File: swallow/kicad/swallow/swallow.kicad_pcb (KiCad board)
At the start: 2 copper layers, 75.8 x 74.2 mm, 36 parts, among them J1 Raspberry Pi 3/4 B, J10 evens, J2 echo2, J3 ground, J4 VCC, J5 echo3, J6 echo4, J7 echo1, J8 power terminal, J9 odds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

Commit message: ++ - kamangir/bolt#746
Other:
- outline, holes or cut-outs redrawn
- board text added: "swallow - v14 Karband / Kamangir"
- board text removed: "swallow - v10 Karband / Kamangir"
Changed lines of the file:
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@@
 	)
 	(gr_circle
-		(center 190.9 117.3)
-		(end 191.8 118.2)
+		(center 190.9 120.8)
+		(end 191.8 121.7)
 		(stroke
 			(width 0.05)
@@
 	)
 	(gr_circle
-		(center 132.9 117.3)
-		(end 133.8 118.2)
+		(center 132.9 120.8)
+		(end 133.8 121.7)
 		(stroke
 			(width 0.05)
@@
 	)
 	(gr_circle
-		(center 132.9 117.3)
-		(end 134.4 114.6)
+		(center 132.9 120.8)
+		(end 134.4 118.1)
 		(stroke
 			(width 0.1)
@@
 	)
 	(gr_circle
-		(center 190.9 117.3)
-		(end 193.1 119.4)
+		(center 190.9 120.8)
+		(end 193.1 122.9)
 		(stroke
 			(width 0.1)
@@
 		)
 	)
-	(gr_text "swallow - v10\nKarband / Kamangir"
+	(gr_text "swallow - v14\nKarband / Kamangir"
 		(at 158.6 63.1 0)
 		(layer "F.SilkS")
@@
 		(layer "User.1")
 		(pts
-			(xy 132.9 117.3) (xy 112.7 87.9)
-		)
-		(height -29.8)
-		(orientation 1)
-		(format
-			(prefix "")
-			(suffix "")
-			(units 3)
-			(units_format 0)
-			(precision 4)
-			(suppress_zeroes yes)
-		)
-		(style
-			(thickness 0.2)
-			(arrow_length 1.27)
-			(text_position_mode 0)
-			(arrow_direction outward)
-			(extension_height 0.58642)
-			(extension_offset 0.5)
-			(keep_text_aligned yes)
-		)
-		(gr_text "29.4"
-			(at 101.95 102.6 90)
-			(layer "User.1")
-			(effects
-				(font
-					(size 1 1)
-					(thickness 0.15)
-				)
-			)
-		)
-	)
-	(dimension
-		(type orthogonal)
-		(layer "User.1")
-		(pts
-			(xy 132.9 71.8) (xy 132.9 117.3)
+			(xy 132.9 71.8) (xy 132.9 120.8)
 		)
 		(height -26.1)
@@
 			(keep_text_aligned yes)
 		)
-		(gr_text "45.5"
-			(at 105.65 94.55 90)
+		(gr_text "49"
+			(at 105.65 96.3 90)
 			(layer "User.1")
 			(effects
@@
 		(layer "User.1")
 		(pts
+			(xy 112.7 87.9) (xy 106.8 120.8)
+		)
+		(height -9.6)
+		(orientation 1)
+		(format
+			(prefix "")
+			(suffix "")
+			(units 3)
+			(units_format 0)
+			(precision 4)
+			(suppress_zeroes yes)
+		)
+		(style
+			(thickness 0.2)
+			(arrow_length 1.27)
+			(text_position_mode 0)
+			(arrow_direction outward)
+			(extension_height 0.58642)
+			(extension_offset 0.5)
+			(keep_text_aligned yes)
+		)
+		(gr_text "32.9"
+			(at 101.95 104.35 90)
+			(layer "User.1")
+			(effects
+				(font
+					(size 1 1)
+					(thickness 0.15)
+				)
+			)
+		)
+	)
+	(dimension
+		(type orthogonal)
+		(layer "User.1")
+		(pts
 			(xy 187.838954 71.8) (xy 193.961046 71.8)
 		)
@@
 		(layer "User.1")
 		(pts
-			(xy 190.9 117.3) (xy 190.9 71.8)
+			(xy 190.9 120.8) (xy 190.9 71.8)
 		)
 		(height 13.6)
@@
 			(keep_text_aligned yes)
 		)
-		(gr_text "45.5"
-			(at 203.35 94.55 90)
-			(layer "User.1")
-			(effects
+		(gr_text "49"
+			(at 203.35 96.3 90)
+			(layer "User.1")
+			(effects

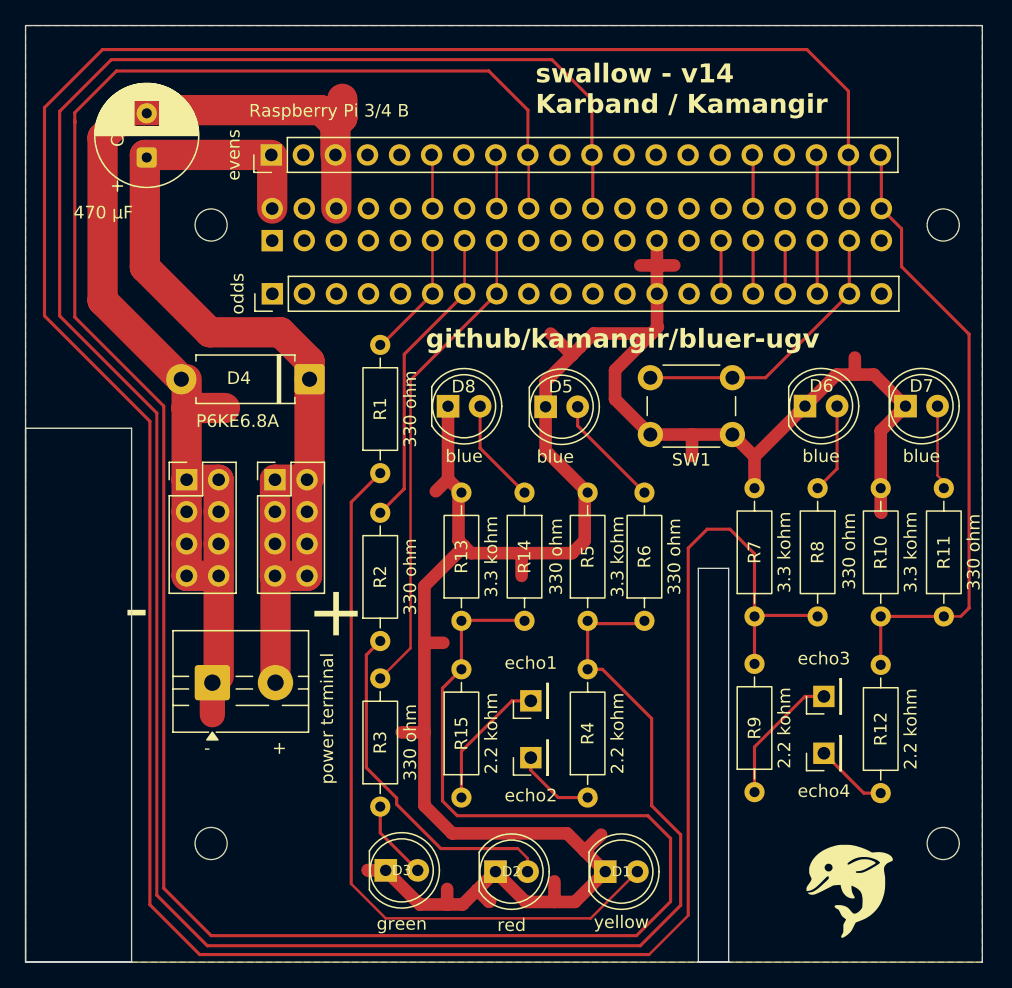
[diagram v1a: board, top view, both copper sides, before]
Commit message: fix - kamangir/bolt#746
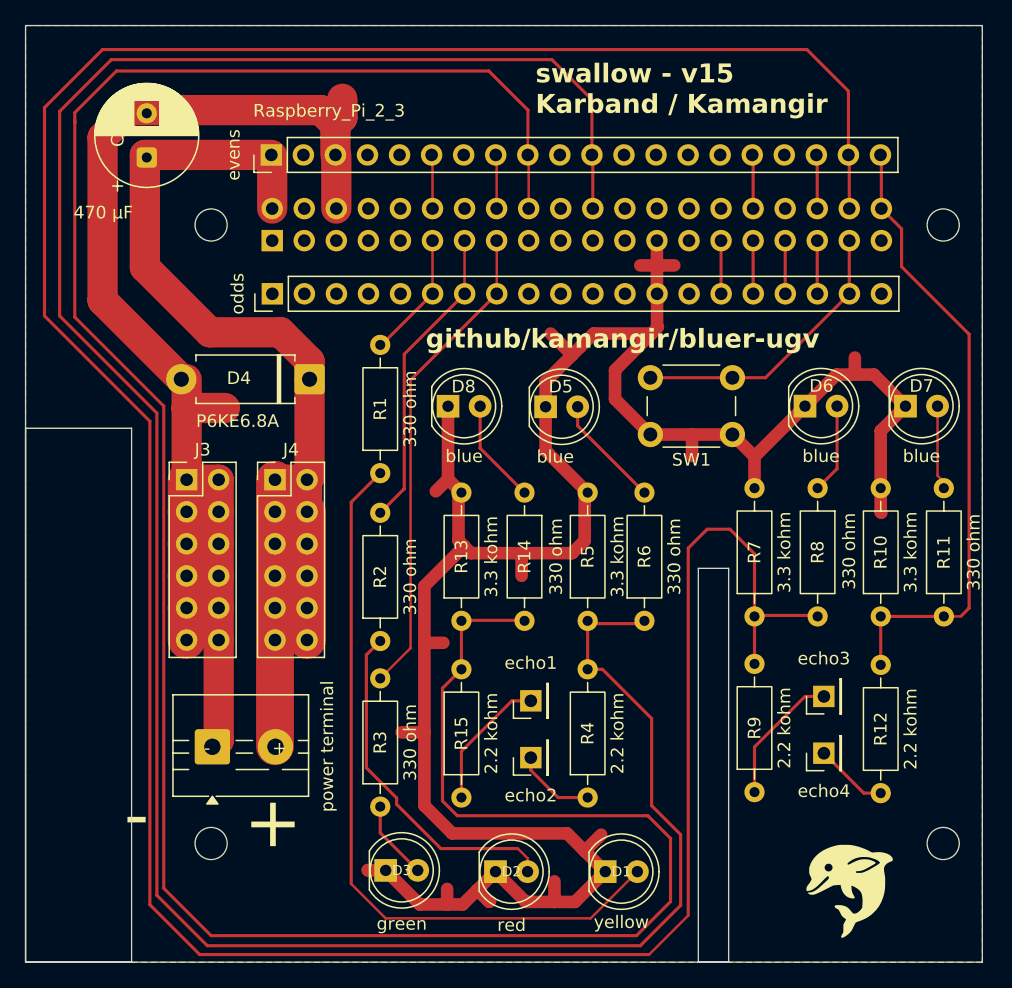
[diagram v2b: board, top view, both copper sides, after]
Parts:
- J1: value Raspberry Pi 3/4 B -> Raspberry_Pi_2_3
- J3, J4: footprint Connector_PinHeader_2.54mm:PinHeader_2x04_P2.54mm_Vertical -> Connector_PinHeader_2.54mm:PinHeader_2x06_P2.54mm_Vertical
- moved J8 5.08 mm to (133.0, 113.1)
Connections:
- C1 pad 2: GND -> Net-(D1-K)
- D1 pad 1: GND -> Net-(D1-K)
- D2 pad 1: GND -> Net-(D1-K)
- D3 pad 1: GND -> Net-(D1-K)
- D4 pad 2: GND -> Net-(D1-K)
- D5 pad 1: GND -> Net-(D1-K)
- D6 pad 1: GND -> Net-(D1-K)
- D7 pad 1: GND -> Net-(D1-K)
- D8 pad 1: GND -> Net-(D1-K)
- J1 pad 25: GND -> Net-(D1-K)
- J1 pad 6: GND -> Net-(D1-K)
- J10 pad 3: GND -> Net-(D1-K)
- J3 pad 1: GND -> Net-(D1-K)
- J3 pad 2: GND -> Net-(D1-K)
- J3 pad 3: GND -> Net-(D1-K)
- J3 pad 4: GND -> Net-(D1-K)
- J3 pad 5: GND -> Net-(D1-K)
- J3 pad 6: GND -> Net-(D1-K)
- J3 pad 7: GND -> Net-(D1-K)
- J3 pad 8: GND -> Net-(D1-K)
- J8 pad 1: GND -> Net-(D1-K)
- J9 pad 13: GND -> Net-(D1-K)
- R10 pad 2: GND -> Net-(D1-K)
- R13 pad 2: GND -> Net-(D1-K)
- R5 pad 2: GND -> Net-(D1-K)
- R7 pad 2: GND -> Net-(D1-K)
- SW1 pad 1: GND -> Net-(D1-K)
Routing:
- net Net-(D1-K): track 0.00 -> 284.5 mm
- net GND: track 276.1 -> 0.00 mm
- net Net-(D4-K): track 77.7 -> 87.9 mm
- added copper zone on F.Cu, net Net-(D1-K)
- removed copper zone on F.Cu, net GND
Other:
- board text added: "swallow - v15 Karband / Kamangir"
- board text removed: "swallow - v14 Karband / Kamangir"

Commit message: ++ - kamangir/bolt#746
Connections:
- C1 pad 1: Net-(D4-K) -> /pin2
- C1 pad 2: Net-(D1-K) -> /pin14
- D1 pad 1: Net-(D1-K) -> /pin14
- D2 pad 1: Net-(D1-K) -> /pin14
- D3 pad 1: Net-(D1-K) -> /pin14
- D4 pad 1: Net-(D4-K) -> /pin2
- D4 pad 2: Net-(D1-K) -> /pin14
- D5 pad 1: Net-(D1-K) -> /pin14
- D6 pad 1: Net-(D1-K) -> /pin14
- D7 pad 1: Net-(D1-K) -> /pin14
- D8 pad 1: Net-(D1-K) -> /pin14
- J1 pad 1: Net-(J1-3V3-Pad1) -> /pin1
- J1 pad 10: unconnected-(J1-GPIO15/RXD-Pad10) -> /pin10
- J1 pad 14: Net-(D1-K) -> /pin14
- J1 pad 17: Net-(J1-3V3-Pad1) -> /pin1
- J1 pad 19: unconnected-(J1-MOSI0/GPIO10-Pad19) -> /pin19
- J1 pad 2: Net-(D4-K) -> /pin2
- J1 pad 20: Net-(D1-K) -> /pin14
- J1 pad 21: unconnected-(J1-MISO0/GPIO9-Pad21) -> /pin21
- J1 pad 23: unconnected-(J1-SCLK0/GPIO11-Pad23) -> /pin23
- J1 pad 24: unconnected-(J1-~{CE0}/GPIO8-Pad24) -> /pin24
- J1 pad 25: Net-(D1-K) -> /pin14
- J1 pad 26: unconnected-(J1-~{CE1}/GPIO7-Pad26) -> /pin26
- J1 pad 27: unconnected-(J1-ID_SD/GPIO0-Pad27) -> /pin27
- J1 pad 28: unconnected-(J1-ID_SC/GPIO1-Pad28) -> /pin28
- J1 pad 3: unconnected-(J1-SDA/GPIO2-Pad3) -> /pin3
- J1 pad 30: Net-(D1-K) -> /pin14
- J1 pad 34: Net-(D1-K) -> /pin14
- J1 pad 39: Net-(D1-K) -> /pin14
- J1 pad 4: Net-(D4-K) -> /pin2
- J1 pad 5: unconnected-(J1-SCL/GPIO3-Pad5) -> /pin5
- J1 pad 6: Net-(D1-K) -> /pin14
- J1 pad 7: unconnected-(J1-GCLK0/GPIO4-Pad7) -> /pin7
- J1 pad 8: unconnected-(J1-GPIO14/TXD-Pad8) -> /pin8
- J1 pad 9: Net-(D1-K) -> /pin14
- J10 pad 1: Net-(D4-K) -> /pin2
- J10 pad 10: unconnected-(J10-Pin_10-Pad10) -> /pin14
- J10 pad 12: unconnected-(J10-Pin_12-Pad12) -> /pin24
- J10 pad 13: unconnected-(J10-Pin_13-Pad13) -> /pin26
- J10 pad 14: unconnected-(J10-Pin_14-Pad14) -> /pin28
- J10 pad 15: unconnected-(J10-Pin_15-Pad15) -> /pin14
- J10 pad 17: unconnected-(J10-Pin_17-Pad17) -> /pin14
- J10 pad 2: unconnected-(J10-Pin_2-Pad2) -> /pin2
- J10 pad 3: Net-(D1-K) -> /pin14
- J10 pad 4: unconnected-(J10-Pin_4-Pad4) -> /pin8
- J10 pad 5: unconnected-(J10-Pin_5-Pad5) -> /pin10
- J10 pad 7: unconnected-(J10-Pin_7-Pad7) -> /pin14
- J3 pad 1: Net-(D1-K) -> /pin14
- J3 pad 10: Net-(D1-K) -> /pin14
- J3 pad 11: Net-(D1-K) -> /pin14
- J3 pad 12: Net-(D1-K) -> /pin14
- J3 pad 2: Net-(D1-K) -> /pin14
- J3 pad 3: Net-(D1-K) -> /pin14
- J3 pad 4: Net-(D1-K) -> /pin14
- J3 pad 5: Net-(D1-K) -> /pin14
- J3 pad 6: Net-(D1-K) -> /pin14
- J3 pad 7: Net-(D1-K) -> /pin14
- J3 pad 8: Net-(D1-K) -> /pin14
- J3 pad 9: Net-(D1-K) -> /pin14
- J4 pad 1: Net-(D4-K) -> /pin2
- J4 pad 10: Net-(D4-K) -> /pin2
- J4 pad 11: Net-(D4-K) -> /pin2
- J4 pad 12: Net-(D4-K) -> /pin2
- J4 pad 2: Net-(D4-K) -> /pin2
- J4 pad 3: Net-(D4-K) -> /pin2
- J4 pad 4: Net-(D4-K) -> /pin2
- J4 pad 5: Net-(D4-K) -> /pin2
- J4 pad 6: Net-(D4-K) -> /pin2
- J4 pad 7: Net-(D4-K) -> /pin2
- J4 pad 8: Net-(D4-K) -> /pin2
- J4 pad 9: Net-(D4-K) -> /pin2
- J8 pad 1: Net-(D1-K) -> /pin14
- J8 pad 2: Net-(D4-K) -> /pin2
- J9 pad 1: unconnected-(J9-Pin_1-Pad1) -> /pin1
- J9 pad 10: unconnected-(J9-Pin_10-Pad10) -> /pin19
- J9 pad 11: unconnected-(J9-Pin_11-Pad11) -> /pin21
- J9 pad 12: unconnected-(J9-Pin_12-Pad12) -> /pin23
- J9 pad 13: Net-(D1-K) -> /pin14
- J9 pad 14: unconnected-(J9-Pin_14-Pad14) -> /pin27
- J9 pad 2: unconnected-(J9-Pin_2-Pad2) -> /pin3
- J9 pad 20: unconnected-(J9-Pin_20-Pad20) -> /pin14
- J9 pad 3: unconnected-(J9-Pin_3-Pad3) -> /pin5
- J9 pad 4: unconnected-(J9-Pin_4-Pad4) -> /pin7
- J9 pad 5: unconnected-(J9-Pin_5-Pad5) -> /pin14
- J9 pad 9: unconnected-(J9-Pin_9-Pad9) -> /pin1
- R10 pad 2: Net-(D1-K) -> /pin14
- R13 pad 2: Net-(D1-K) -> /pin14
- R5 pad 2: Net-(D1-K) -> /pin14
- R7 pad 2: Net-(D1-K) -> /pin14
- SW1 pad 1: Net-(D1-K) -> /pin14
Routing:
- net /pin14: track 0.00 -> 341.0 mm
- net Net-(D1-K): track 284.5 -> 0.00 mm
- net /pin2: track 0.00 -> 97.2 mm
- net Net-(D4-K): track 87.9 -> 0.00 mm
- net /pin1: track 0.00 -> 8.43 mm
- net /pin8: track 0.00 -> 4.28 mm
- net /pin28: track 0.00 -> 4.28 mm
- net /pin26: track 0.00 -> 4.28 mm
- net /pin24: track 0.00 -> 4.28 mm
- net /pin10: track 0.00 -> 4.28 mm
- net /pin27: track 0.00 -> 4.21 mm
- net /pin5: track 0.00 -> 4.21 mm
- net /pin21: track 0.00 -> 4.21 mm
- net /pin19: track 0.00 -> 4.21 mm
- net /pin7: track 0.00 -> 4.21 mm
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- added copper zone on F.Cu, net /pin14
- removed copper zone on F.Cu, net Net-(D1-K)
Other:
- board text added: "swallow - v16 Karband / Kamangir"
- board text removed: "swallow - v15 Karband / Kamangir"

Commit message: ++
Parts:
- J1: value Raspberry_Pi_2_3 -> Raspberry Pi: 0, 3, 4 or 5
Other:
- board text added: "swallow - v17 Karband / Kamangir"
- board text removed: "swallow - v16 Karband / Kamangir"
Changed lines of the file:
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@@
 			)
 		)
-		(property "Value" "Raspberry_Pi_2_3"
+		(property "Value" "Raspberry Pi: 0, 3, 4 or 5"
 			(at -10.29 -4.51 180)
 			(layer "F.SilkS")
@@
 		)
 	)
-	(gr_text "swallow - v16\nKarband / Kamangir"
+	(gr_text "swallow - v17\nKarband / Kamangir"
 		(at 158.6 63.1 0)
 		(layer "F.SilkS")
